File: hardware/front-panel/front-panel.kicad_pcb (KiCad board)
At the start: 4 copper layers, 180 x 100 mm, 76 parts, among them J1 Conn_02x20_Odd_Even, J10 SMA, J11 SMA, J12 SMA, J13 SMA, J14 SMA, J15 SMA, J16 SMA, J17 SMA, J18 SMA, J19 SMA, J2 Conn_02x20_Odd_Even, J20 SMA, J21 SMA, J22 SMA, J23 SMA, J24 SMA, J25 SMA, J3 Conn_02x20_Odd_Even, J30 OLED 0.96in module on 1x4 soc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, J31 KF128-2.54-10P, J32 KF128-5.0-2P, J33 Qwiic (vertical), J40 Module header 2x6 (shrouded), J411 KF301-5.0-2P, J412 KF301-5.0-2P, Q411 MMBT5551, Q412 MMBT5551, Q421 MMBT5551, Q422 MMBT5551, U401 6N137S-TA1-L, U402 6N137S-TA1-L, U410 SN74AHCT541PWR

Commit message: Schematic review fixes, part 2 (Konnect): panel RX/AUX labels + SMA labels swapped to match the main board (copper unchanged); TX_VMID -> R820 47k -> TX_IN (C810 couples into TX_IN); Q901 D/S corrected + D932 to +VEXT; R950 10k Q904 gate-source; R712 permanent (J3 pin 1 tied to pin 2); U302/C308 on +5VA; panel 6N137 VCC/VE + C401/C402 on +5V_RAW; R521-R528 DIO pull-downs; front_panel_link sheet removed from the root; change notes on six sheets; panel silk: pairing labels corrected, stale J3 texts deleted, TX/RX/AUX labels fixed, OUT1..7. ERC unchanged (2 cosmetic), panel DRC 0/0; netlist diff = intended changes only
Co-Authored-By: Claude Fable 5.1 <noreply@anthropic.com>
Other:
- board text added: "1,2 = +5V 3..9 = OUT1..7 10 = spare 11,12 = GND relay / H-bridge"
- board text added: "J1 = J6"
- board text added: "J2 = J8"
- board text added: "J3 = J7"
- board text added: "TX"
- board text removed: "1,2 = +5V 3..10 = OUT1..8 11,12 = GND relay / H-bridge"
- board text removed: "J2 = J7"
- board text removed: "J3"
- board text removed: "J3 = J6"
- board text removed: "J3 = J8"
- board text removed: "J3 pin 40"
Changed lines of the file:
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@@
 		)
 	)
-	(gr_text "J3 = J6"
-		(at 7 83.15 0)
-		(layer "F.SilkS")
-		(effects
-			(font
-				(size 1 1)
-				(thickness 0.15)
-			)
-		)
-	)
-	(gr_text "1,2 = +5V   3..10 = OUT1..8   11,12 = GND   relay / H-bridge"
-		(at 45.4 53.55 0)
-		(layer "F.SilkS")
-		(effects
-			(font
-				(size 1 1)
-				(thickness 0.15)
-			)
-		)
-	)
 	(gr_text "ISO IN 2  5-24 V"
 		(at 61.525001 81.085 0)
@@
 		)
 	)
-	(gr_text "J2 = J7"
-		(at 173 104.4 0)
-		(layer "F.SilkS")
-		(effects
-			(font
-				(size 1 1)
-				(thickness 0.15)
-			)
-		)
-	)
-	(gr_text "J3 = J8"
-		(at 54.375003 103.205 90)
-		(layer "F.SilkS")
-		(effects
-			(font
-				(size 1 1)
-				(thickness 0.15)
-			)
-		)
-	)
 	(gr_text "+"
 		(at 56.875002 105.305 90)
@@
 		)
 	)
-	(gr_text "J3 = J8"
-		(at 81.850002 103.28 90)
-		(layer "F.SilkS")
-		(effects
-			(font
-				(size 1 1)
-				(thickness 0.15)
-			)
-		)
-	)
 	(gr_text "+"
 		(at 84.350001 105.38 90)
@@
 		)
 	)
-	(gr_text "AUX"
-		(at 111.65 67.27 0)
-		(layer "F.SilkS")
-		(effects
-			(font
-				(size 1.2 1.2)
-				(thickness 0.2)
-			)
-		)
-	)
 	(gr_text "AI7"
 		(at 111.7 49 0)
@@
 		)
 	)
-	(gr_text "RX"
-		(at 147.65 31.57 0)
-		(layer "F.SilkS")
-		(effects
-			(font
-				(size 1.2 1.2)
-				(thickness 0.2)
-			)
-		)
-	)
 	(gr_text "FAST2"
 		(at 165.75 49.3 0)
@@
 		)
 	)
-	(gr_text "J3 pin 40"
-		(at 52.645002 103.205 90)
-		(layer "B.SilkS")
-		(effects
-			(font
-				(size 1 1)
-				(thickness 0.15)
-			)
-			(justify mirror)
-		)
-	)
-	(gr_text "J3 pin 40"
-		(at 80.120001 103.28 90)
-		(layer "B.SilkS")
-		(effects
-			(font
-				(size 1 1)
-				(thickness 0.15)
-			)
-			(justify mirror)
-		)
-	)
 	(gr_text "REAR / TOP EDGE"
 		(at 114.9 16.75 0)
@@
 		)
 	)
-	(gr_text "J3"
-		(at 78.250001 103.28 0)
-		(layer "B.Fab")
-		(effects
-			(font
-				(size 1 1)
-				(thickness 0.15)
-			)
-			(justify mirror)
-		)
-	)
 	(segment
 		(start 64.4 100.999998)
@@
 	)
 	(embedded_fonts no)
-)
+  (gr_text "J3 = J7"
+    (at 7 83.2 0)
+    (layer "F.SilkS")
+    (effects (font (size 1 1) (thickness 0.15)))
+  )
+  (gr_text "J2 = J8"
+    (at 173 104.4 0)
+    (layer "F.SilkS")
+    (effects (font (size 1 1) (thickness 0.15)))
+  )
+  (gr_text "J1 = J6"
+    (at 70 17 0)
+    (layer "F.SilkS")
+    (effects (font (size 1 1) (thickness 0.15)))
+  )
+  (gr_text "1,2 = +5V   3..9 = OUT1..7   10 = spare   11,12 = GND   relay / H-bridge"
+    (at 45.4 53.5 0)
+    (layer "F.SilkS")
+    (effects (font (size 1 1) (thickness 0.15)))
+  )
+  (gr_text "TX"
+    (at 111.7 67.3 0)
+    (layer "F.SilkS")
+    (effects (font (size 1 1) (thickness 0.15)))
+  )
+  (gr_text "AUX"
+    (at 147.7 31.6 0)
+    (layer "F.SilkS")
+    (effects (font (size 1 1) (thickness 0.15)))
+  )
+  (gr_text "RX"
+    (at 147.7 49 0)
+    (layer "F.SilkS")
+    (effects (font (size 1 1) (thickness 0.15)))
+  ))

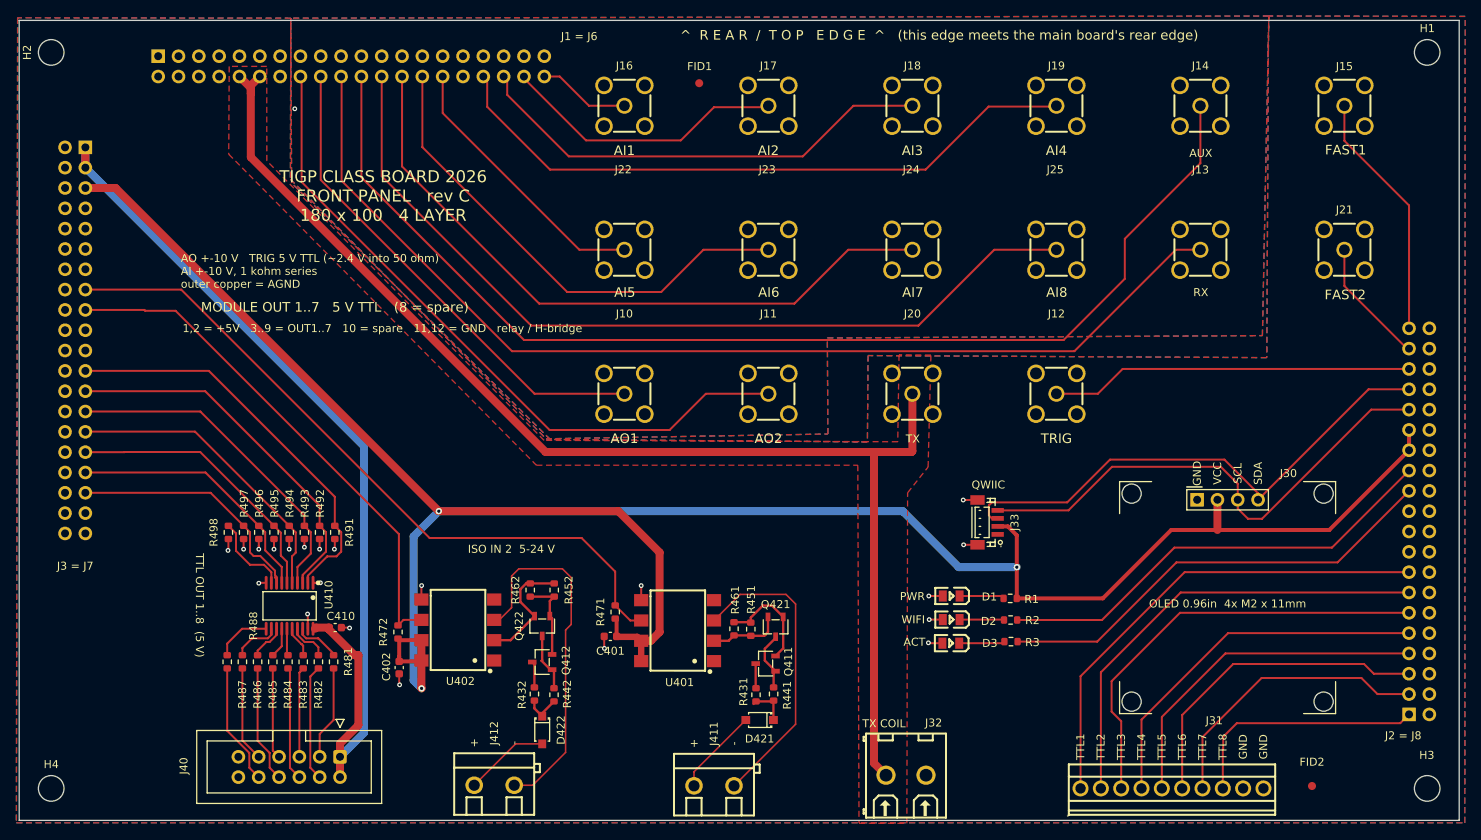
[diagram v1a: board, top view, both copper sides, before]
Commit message: hardware: instructor 2026-10-01 saves synced (one GND net on both boards, PCB updated, R951-R958, headers DNP per Decision #73) + nmr_tx R808 -> TX_VMID, C813 removed, R805/R806 10 k (review B2)
Co-Authored-By: Claude Fable 5.1 <noreply@anthropic.com>
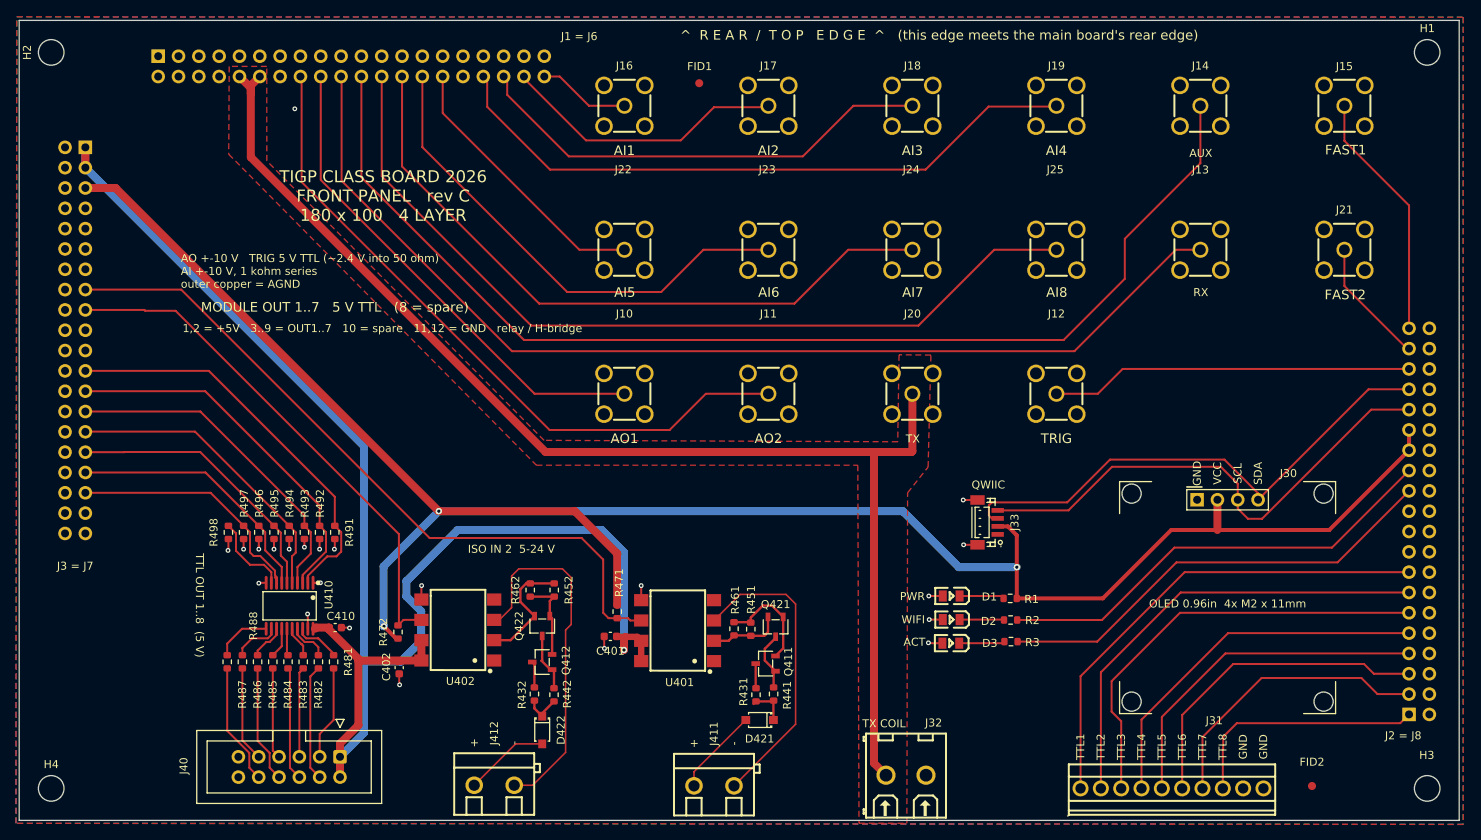
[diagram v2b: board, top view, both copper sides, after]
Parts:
- moved R471 0.25 mm to (74.8, 88.9), turned to -90 degrees
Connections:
- C401 pad 1: +3V3 -> +5V_RAW
- C402 pad 1: +3V3 -> +5V_RAW
- J1 pad 13: unconnected-(J1-Pin_13-Pad13) -> GND
- J1 pad 15: AGND -> GND
- J1 pad 17: AGND -> GND
- J1 pad 19: AGND -> GND
- J1 pad 20: /AUX -> /RX
- J1 pad 21: AGND -> GND
- J1 pad 22: /RX -> /AUX
- J1 pad 23: AGND -> GND
- J1 pad 25: AGND -> GND
- J1 pad 27: AGND -> GND
- J1 pad 29: AGND -> GND
- J1 pad 31: AGND -> GND
- J1 pad 33: AGND -> GND
- J1 pad 35: AGND -> GND
- J1 pad 37: AGND -> GND
- J1 pad 39: AGND -> GND
- J10 pad 1: AGND -> GND
- J10 pad 2: AGND -> GND
- J10 pad 3: AGND -> GND
- J10 pad 4: AGND -> GND
- J11 pad 1: AGND -> GND
- J11 pad 2: AGND -> GND
- J11 pad 3: AGND -> GND
- J11 pad 4: AGND -> GND
- J13 pad 1: AGND -> GND
- J13 pad 2: AGND -> GND
- J13 pad 3: AGND -> GND
- J13 pad 4: AGND -> GND
- J13 pad 5: /AUX -> /RX
- J14 pad 1: AGND -> GND
- J14 pad 2: AGND -> GND
- J14 pad 3: AGND -> GND
- J14 pad 4: AGND -> GND
- J14 pad 5: /RX -> /AUX
- J16 pad 1: AGND -> GND
- J16 pad 2: AGND -> GND
- J16 pad 3: AGND -> GND
- J16 pad 4: AGND -> GND
- J17 pad 1: AGND -> GND
- J17 pad 2: AGND -> GND
- J17 pad 3: AGND -> GND
- J17 pad 4: AGND -> GND
- J18 pad 1: AGND -> GND
- J18 pad 2: AGND -> GND
- J18 pad 3: AGND -> GND
- J18 pad 4: AGND -> GND
- J19 pad 1: AGND -> GND
- J19 pad 2: AGND -> GND
- J19 pad 3: AGND -> GND
- J19 pad 4: AGND -> GND
- J22 pad 1: AGND -> GND
- J22 pad 2: AGND -> GND
- J22 pad 3: AGND -> GND
- J22 pad 4: AGND -> GND
- J23 pad 1: AGND -> GND
- J23 pad 2: AGND -> GND
- J23 pad 3: AGND -> GND
- J23 pad 4: AGND -> GND
- J24 pad 1: AGND -> GND
- J24 pad 2: AGND -> GND
- J24 pad 3: AGND -> GND
- J24 pad 4: AGND -> GND
- J25 pad 1: AGND -> GND
- J25 pad 2: AGND -> GND
- J25 pad 3: AGND -> GND
- J25 pad 4: AGND -> GND
- U401 pad 7: +3V3 -> +5V_RAW
- U401 pad 8: +3V3 -> +5V_RAW
- U402 pad 7: +3V3 -> +5V_RAW
- U402 pad 8: +3V3 -> +5V_RAW
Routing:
- net +5V_RAW: track 120.2 -> 197.7 mm, vias 0 -> 1
- net +3V3: track 299.0 -> 260.3 mm
- net /RX: track 145.2 -> 134.5 mm
- net /AUX: track 134.5 -> 145.2 mm
- net /OPTO_IN1: track 89.1 -> 90.5 mm
- net GND: vias 21 -> 22
- net AGND: vias 1 -> 0
- removed copper zone on B.Cu, net AGND
- removed copper zone on F.Cu, net AGND
- removed copper zone on In1.Cu, net AGND
- removed copper zone on In2.Cu, net AGND
